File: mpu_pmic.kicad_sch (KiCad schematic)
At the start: 60 parts, among them J501 EMI shield frame, U501 STPMIC1DPQR

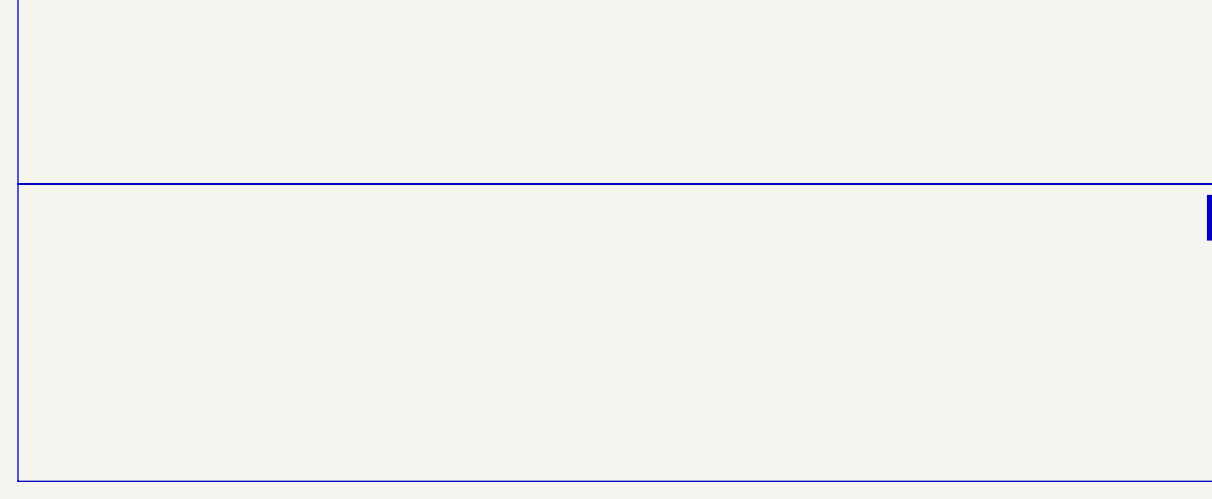
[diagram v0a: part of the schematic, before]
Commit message: Switching freq is 2 MHz, update EMI filter
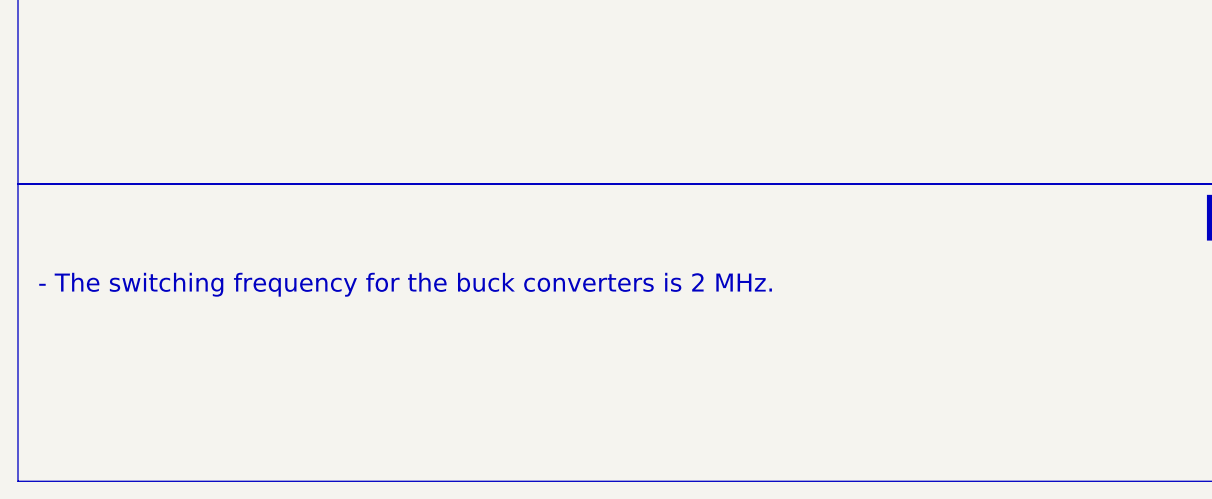
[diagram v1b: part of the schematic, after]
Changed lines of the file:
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@@
+		)
+	)
+	(text_box "- The switching frequency for the buck converters is 2 MHz."
+		(exclude_from_sim no)
+		(at 13.97 260.35 0)
+		(size 283.21 22.86)
+		(margins 0.9525 0.9525 0.9525 0.9525)
+		(stroke
+			(width -0.0001)
+			(type solid)
+		)
+		(fill
+			(type none)
+		)
+		(effects
+			(font
+				(size 2 2)
+			)
+			(justify left top)
 		)
 	)

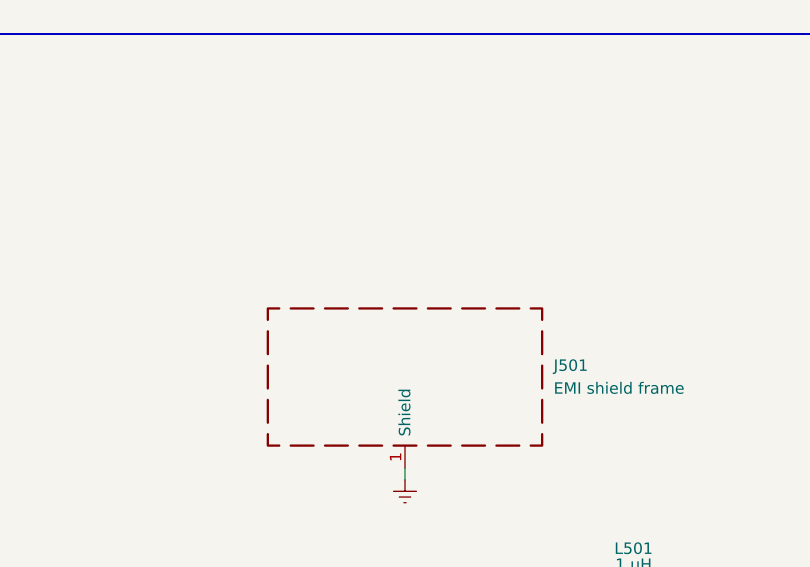
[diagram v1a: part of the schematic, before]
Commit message: Connect ESD TVS to chassis where possible, update version and date
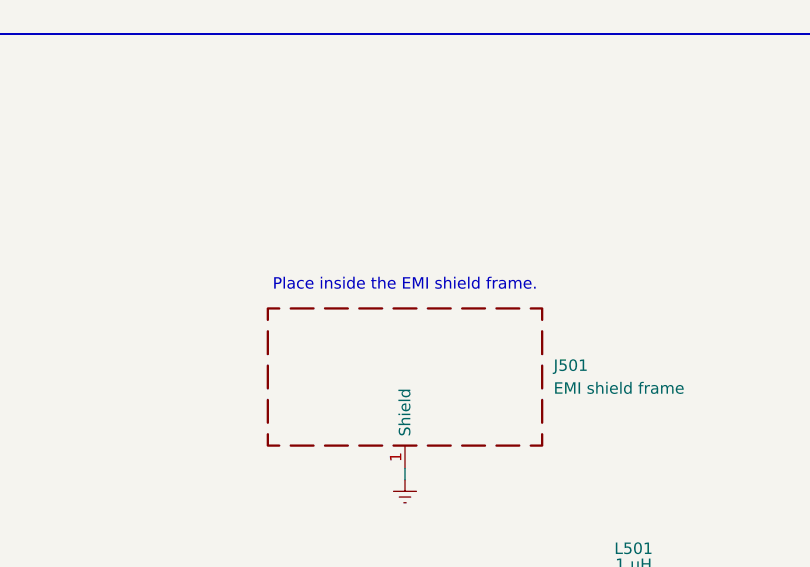
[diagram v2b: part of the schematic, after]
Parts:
- J501: footprint RF_Shielding:Laird_Technologies_BMI-S-202-F_16.50x16.50mm -> RF_Shielding:Laird_Technologies_BMI-S-203-F_26.21x26.21mm
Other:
- note added: "Place inside the EMI shield frame."
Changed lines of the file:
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@@
 	(title_block
 		(title "Linux SBC")
-		(date "2025-11-07")
-		(rev "v0.0.1")
+		(date "2025-12-14")
+		(rev "v1.0.0")
 	)
 	(bus_alias "PMIC"
@@
 		)
 	)
+	(text "Place inside the EMI shield frame."
+		(exclude_from_sim no)
+		(at 182.88 78.74 0)
+		(effects
+			(font
+				(size 1.27 1.27)
+			)
+		)
+	)
 	(text_box "Notes"
 		(exclude_from_sim no)
@@
 			)
 		)
-		(property "Footprint" "RF_Shielding:Laird_Technologies_BMI-S-202-F_16.50x16.50mm"
+		(property "Footprint" "RF_Shielding:Laird_Technologies_BMI-S-203-F_26.21x26.21mm"
 			(at 182.88 91.44 0)
 			(effects

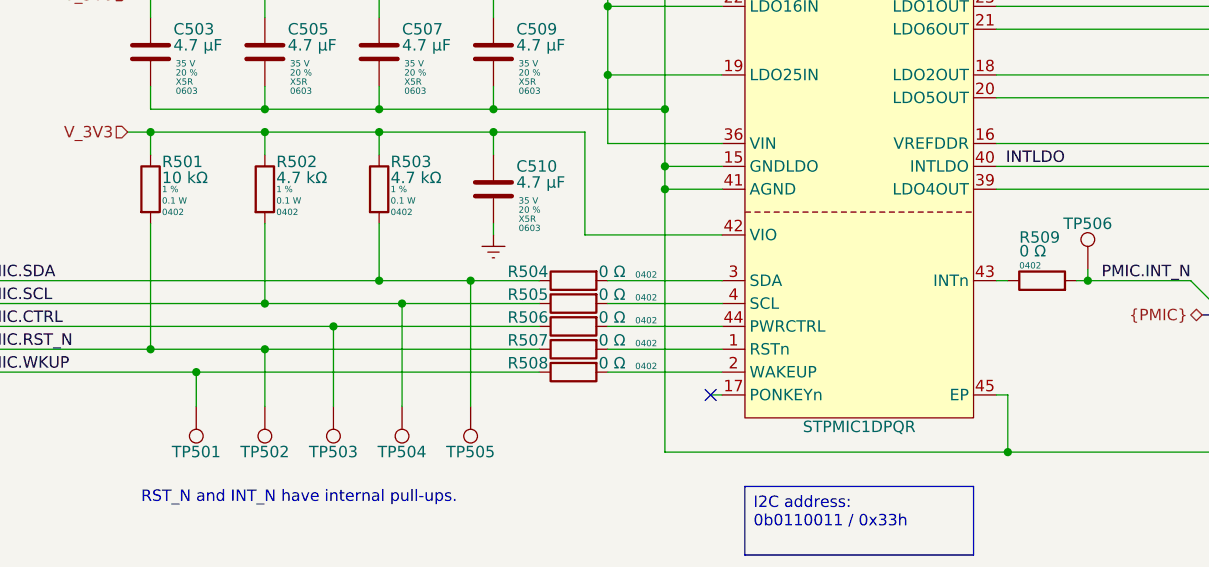
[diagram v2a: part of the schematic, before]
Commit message: 0402 -> 0201 where possible
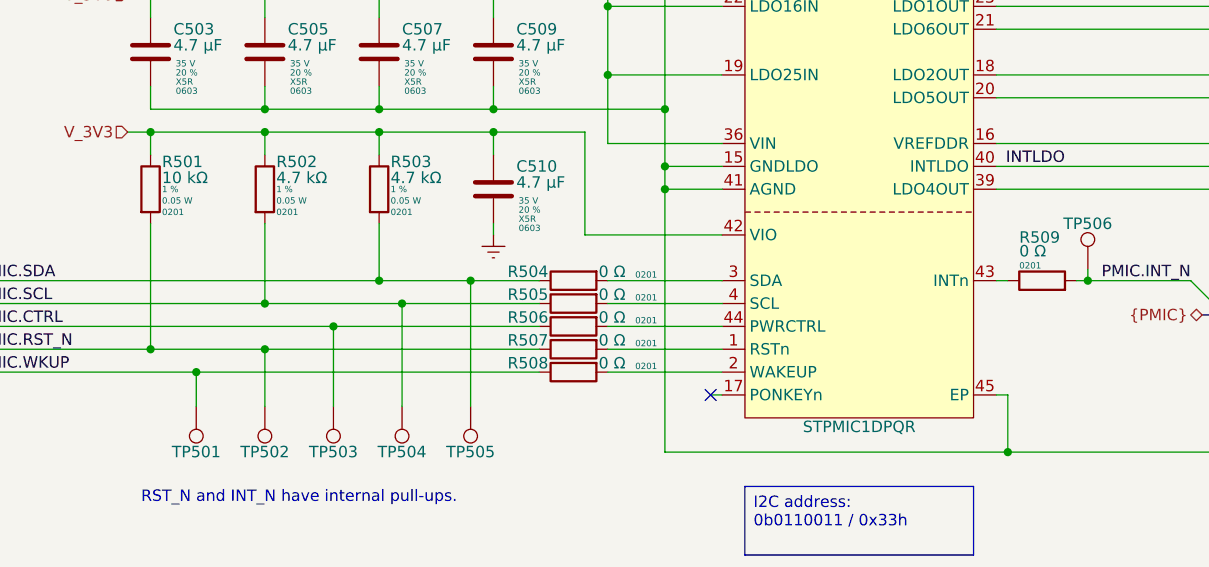
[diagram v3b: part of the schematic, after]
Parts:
- R501: footprint perfect_footprints:R_0402_1005Metric -> Resistor_SMD:R_0201_0603Metric; Digi-Key Part Number P10.0KLCT-ND -> P122414CT-ND; MPN ERJ-2RKF1002X -> ERJ-1GNF1002C; Power rating 0.1 W -> 0.05 W; Size 0402 -> 0201
- R502, R503: footprint perfect_footprints:R_0402_1005Metric -> Resistor_SMD:R_0201_0603Metric; Digi-Key Part Number P4.70KLCT-ND -> P123031CT-ND; MPN ERJ-2RKF4701X -> ERJ-1GNF4701C; Power rating 0.1 W -> 0.05 W; Size 0402 -> 0201
- R504, R505, R506, R507, R508, R509: footprint perfect_footprints:R_0402_1005Metric -> Resistor_SMD:R_0201_0603Metric; Digi-Key Part Number P0.0JCT-ND -> P15979CT-ND; MPN ERJ-2GE0R00X -> ERJ-1GN0R00C; Size 0402 -> 0201

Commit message: Update BOM, and fix MPU pinout
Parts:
- R501, R502, R503, R504, R505, R506, R507, R508, R509: footprint Resistor_SMD:R_0201_0603Metric -> perfect_footprints:R_0201_0603Metric
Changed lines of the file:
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@@
 			)
 		)
-		(property "Footprint" "Resistor_SMD:R_0201_0603Metric"
+		(property "Footprint" "perfect_footprints:R_0201_0603Metric"
 			(at 151.13 196.342 90)
 			(effects
@@
 			)
 		)
-		(property "Footprint" "Resistor_SMD:R_0201_0603Metric"
+		(property "Footprint" "perfect_footprints:R_0201_0603Metric"
 			(at 151.13 198.882 90)
 			(effects
@@
 			)
 		)
-		(property "Footprint" "Resistor_SMD:R_0201_0603Metric"
+		(property "Footprint" "perfect_footprints:R_0201_0603Metric"
 			(at 203.2 194.818 90)
 			(effects
@@
 			)
 		)
-		(property "Footprint" "Resistor_SMD:R_0201_0603Metric"
+		(property "Footprint" "perfect_footprints:R_0201_0603Metric"
 			(at 115.062 182.88 90)
 			(effects
@@
 			)
 		)
-		(property "Footprint" "Resistor_SMD:R_0201_0603Metric"
+		(property "Footprint" "perfect_footprints:R_0201_0603Metric"
 			(at 151.13 201.422 90)
 			(effects
@@
 			)
 		)
-		(property "Footprint" "Resistor_SMD:R_0201_0603Metric"
+		(property "Footprint" "perfect_footprints:R_0201_0603Metric"
 			(at 151.13 193.802 90)
 			(effects
@@
 			)
 		)
-		(property "Footprint" "Resistor_SMD:R_0201_0603Metric"
+		(property "Footprint" "perfect_footprints:R_0201_0603Metric"
 			(at 151.13 191.262 90)
 			(effects
@@
 			)
 		)
-		(property "Footprint" "Resistor_SMD:R_0201_0603Metric"
+		(property "Footprint" "perfect_footprints:R_0201_0603Metric"
 			(at 127.762 182.88 90)
 			(effects
@@
 			)
 		)
-		(property "Footprint" "Resistor_SMD:R_0201_0603Metric"
+		(property "Footprint" "perfect_footprints:R_0201_0603Metric"
 			(at 102.362 182.88 90)
 			(effects
